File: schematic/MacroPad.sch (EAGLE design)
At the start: 70 parts, among them IC1 MIC5219BM5, J1 USB4085-GF-A_REVA4, U1 ATMEGA32U4-AUR, Y1 XRCGB16M000FXN00R0

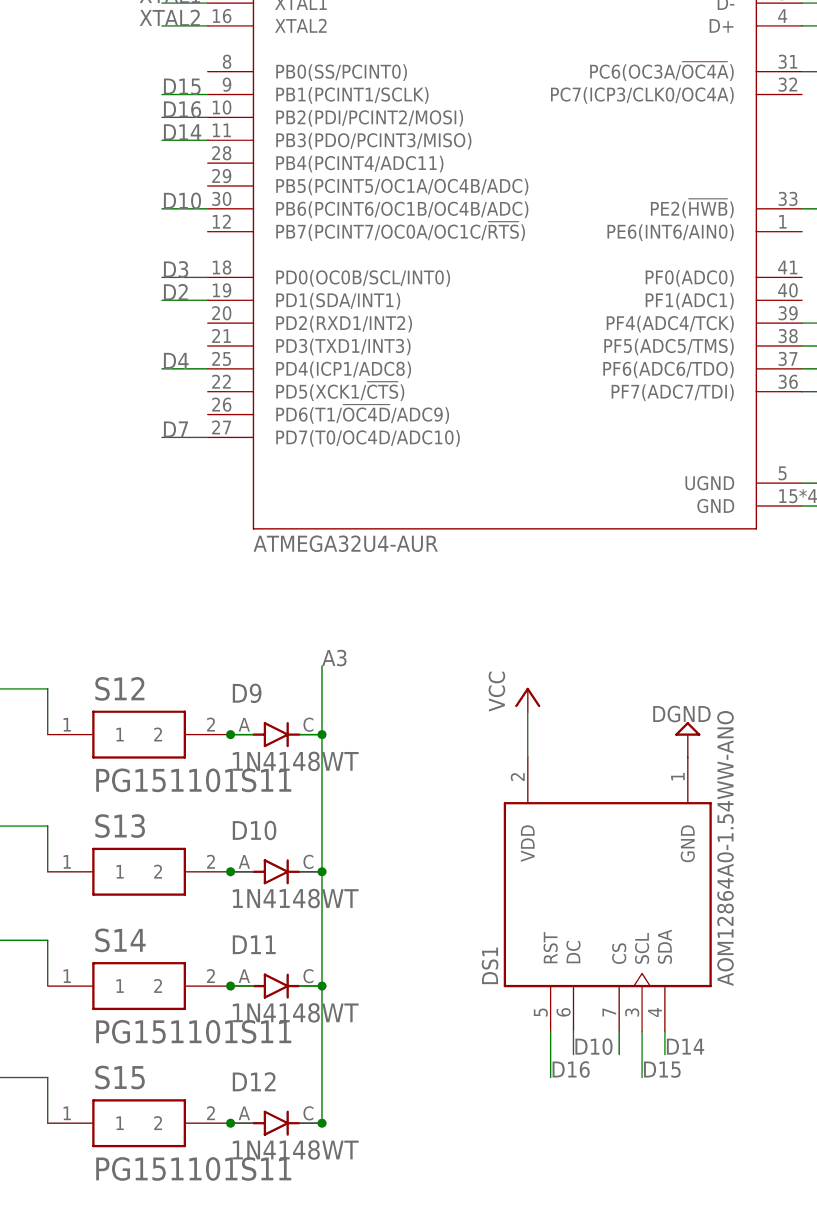
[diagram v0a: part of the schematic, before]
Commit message: Added CS pin for display to schematic + board
The CS pin was initially left not connected intentionally, because I was led to believe that the CS pin was only needed when using multiple devices on SPI. However, for displays like the one used, the CS pin is needed for proper display initialization. DO NOT use earlier schematics and/or board files, as these do not have a properly working display connector.
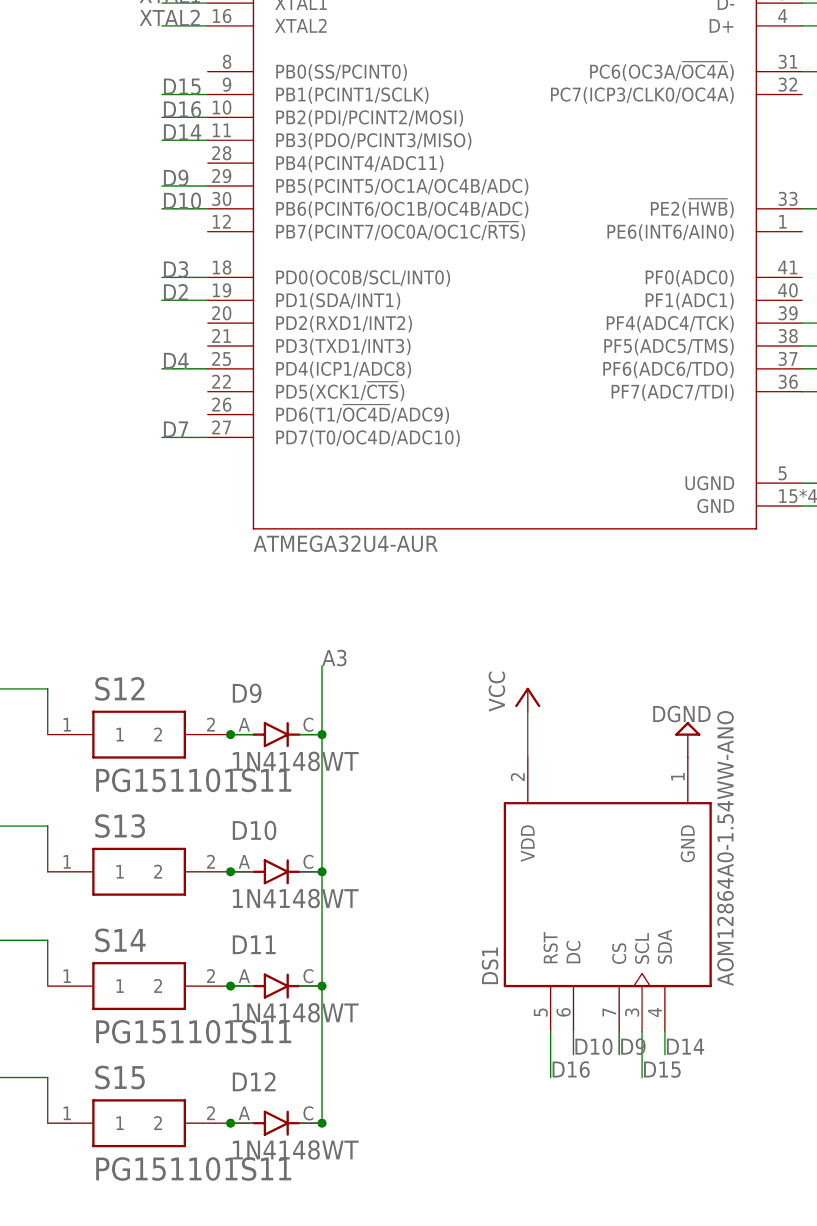
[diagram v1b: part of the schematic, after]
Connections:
- removed net N$24: DS1.CS
- new net D9: DS1.CS, U1.PB5(PCINT5/OC1A/OC4B/ADC)
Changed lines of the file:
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@@
 </segment>
 </net>
-<net name="N$24" class="0">
+<net name="D9" class="0">
 <segment>
 <pinref part="DS1" gate="G$1" pin="CS"/>
 <wire x1="226.06" y1="17.78" x2="226.06" y2="15.24" width="0.1524" layer="91"/>
+<label x="226.06" y="15.24" size="1.778" layer="95"/>
+</segment>
+<segment>
+<pinref part="U1" gate="G$1" pin="PB5(PCINT5/OC1A/OC4B/ADC)"/>
+<wire x1="180.34" y1="111.76" x2="175.26" y2="111.76" width="0.1524" layer="91"/>
+<label x="175.26" y="111.76" size="1.778" layer="95"/>
 </segment>
 </net>
